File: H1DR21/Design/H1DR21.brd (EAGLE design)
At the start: 34.6 x 30 mm, 25 parts, among them P2 HEXABIT_17.32_NO_P6, U1 STM32G0B1CEU6QFN_B1CEU6_STM-L, U2 TCAN334DCNT, X1 XTALL_CSTCE8M00G52

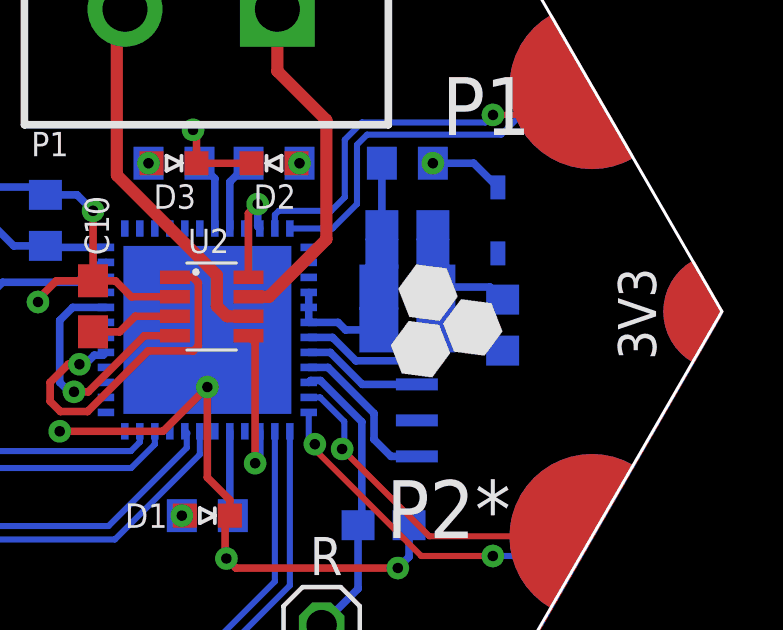
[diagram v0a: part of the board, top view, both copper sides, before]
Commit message: - Changed logo in layout - Rearranged components in BOM
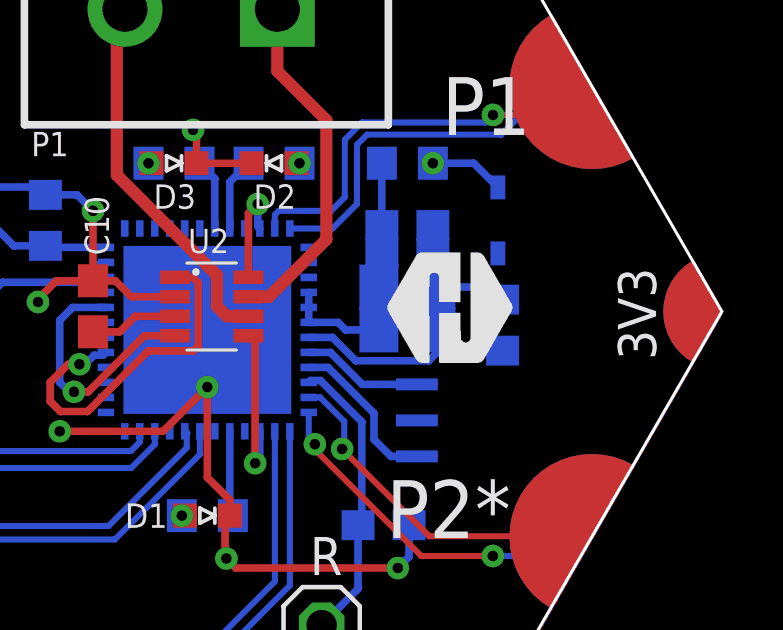
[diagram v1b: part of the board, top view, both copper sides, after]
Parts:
- added U$1: (no value), HEXABITZ_USER_INTERFACE_PARTS:HEXA-LOGO
